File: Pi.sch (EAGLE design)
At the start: 9 parts, among them X1 RASPI_GPIO_B+#_BOX, X2 HDD, 5V 700mA

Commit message: Pi und Stromversorgung Rev. 2019
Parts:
- removed SV1: PLATINENVERBINDER-31SMD, homepi:PLATINENVERBINDER-31SMD
- added JP2: (no value), pinhead:PINHD-1X1
- added X3: MAC64L, con-vg:MAC64L
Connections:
- new net +24V: X3.A32, X3.C32
- new net +5V_EXT: X3.A31, X3.C31
- new net GND_EXT: X3.A30, X3.C30
- new net PI_RESET: JP2.1, X3.C7
- new net RXD: X1.RXD, X3.C27
- new net TXD: X1.TXD, X3.C26
- net +3,3V: now also X3.A2, X3.C2; no longer SV1.2
- net +5V_INT: now also X3.A1, X3.C1; no longer SV1.1
- net +5V_INT2: now also X3.A28, X3.C28; no longer SV1.28
- net 1WIRE: now also X3.A7; no longer SV1.7
- net GND_INT: now also X3.A29, X3.A3, X3.A6, X3.A8, X3.C29, X3.C3, X3.C6, X3.C8; no longer SV1.29, SV1.3, SV1.6, SV1.8
- net GPIO.05: now also X3.A14; no longer SV1.14
- net GPIO.06: now also X3.A15; no longer SV1.15
- net GPIO.12: now also X3.A16; no longer SV1.16
- net GPIO.13: now also X3.A17; no longer SV1.17
- net GPIO.16: now also X3.A18; no longer SV1.18
- net GPIO.17: now also X3.A19; no longer SV1.19
- net GPIO.18: now also X3.A20; no longer SV1.20
- net GPIO.19: now also X3.A21; no longer SV1.21
- net GPIO.20: now also X3.A22; no longer SV1.22
- net GPIO.21: now also X3.A23; no longer SV1.23
- net GPIO.22: now also X3.A24; no longer SV1.24
- net GPIO.23: now also X3.A25; no longer SV1.25
- net GPIO.24: now also X3.A26; no longer SV1.26
- net GPIO.25: now also X3.A27; no longer SV1.27
- net I2C_SCL: now also X3.A5; no longer SV1.5
- net I2C_SDA: now also X3.A4; no longer SV1.4
- net SPI_CE0: now also X3.A12; no longer SV1.12
- net SPI_CE1: now also X3.A13; no longer SV1.13
- net SPI_MISO: now also X3.A10; no longer SV1.10
- net SPI_MOSI: now also X3.A9; no longer SV1.9
- net SPI_SCLK: now also X3.A11; no longer SV1.11
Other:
- note added: "Einschubplatine für den Raspberry Pi Rev. 2019/03"
- moved on the sheet: JP1, LED1, LED2, R1, R2, RPI1, X2-1, X2-2

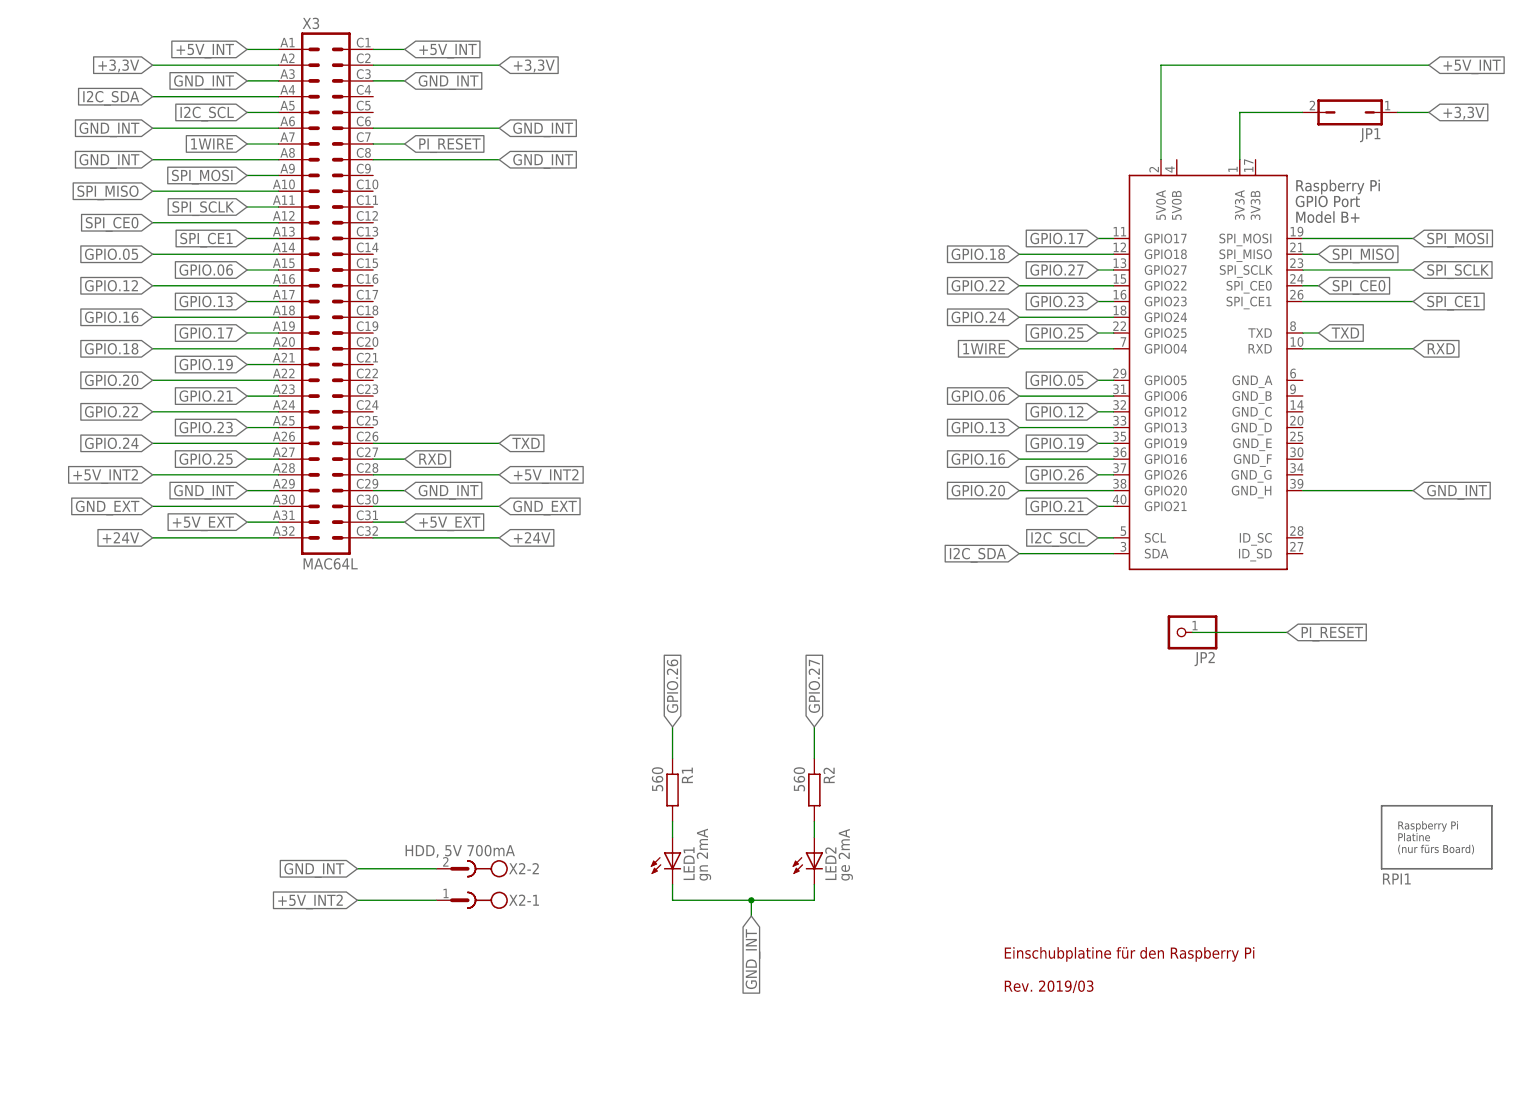
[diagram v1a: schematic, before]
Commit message: Anpassungen an Rev. 2019, erste Can-Bus Elemente
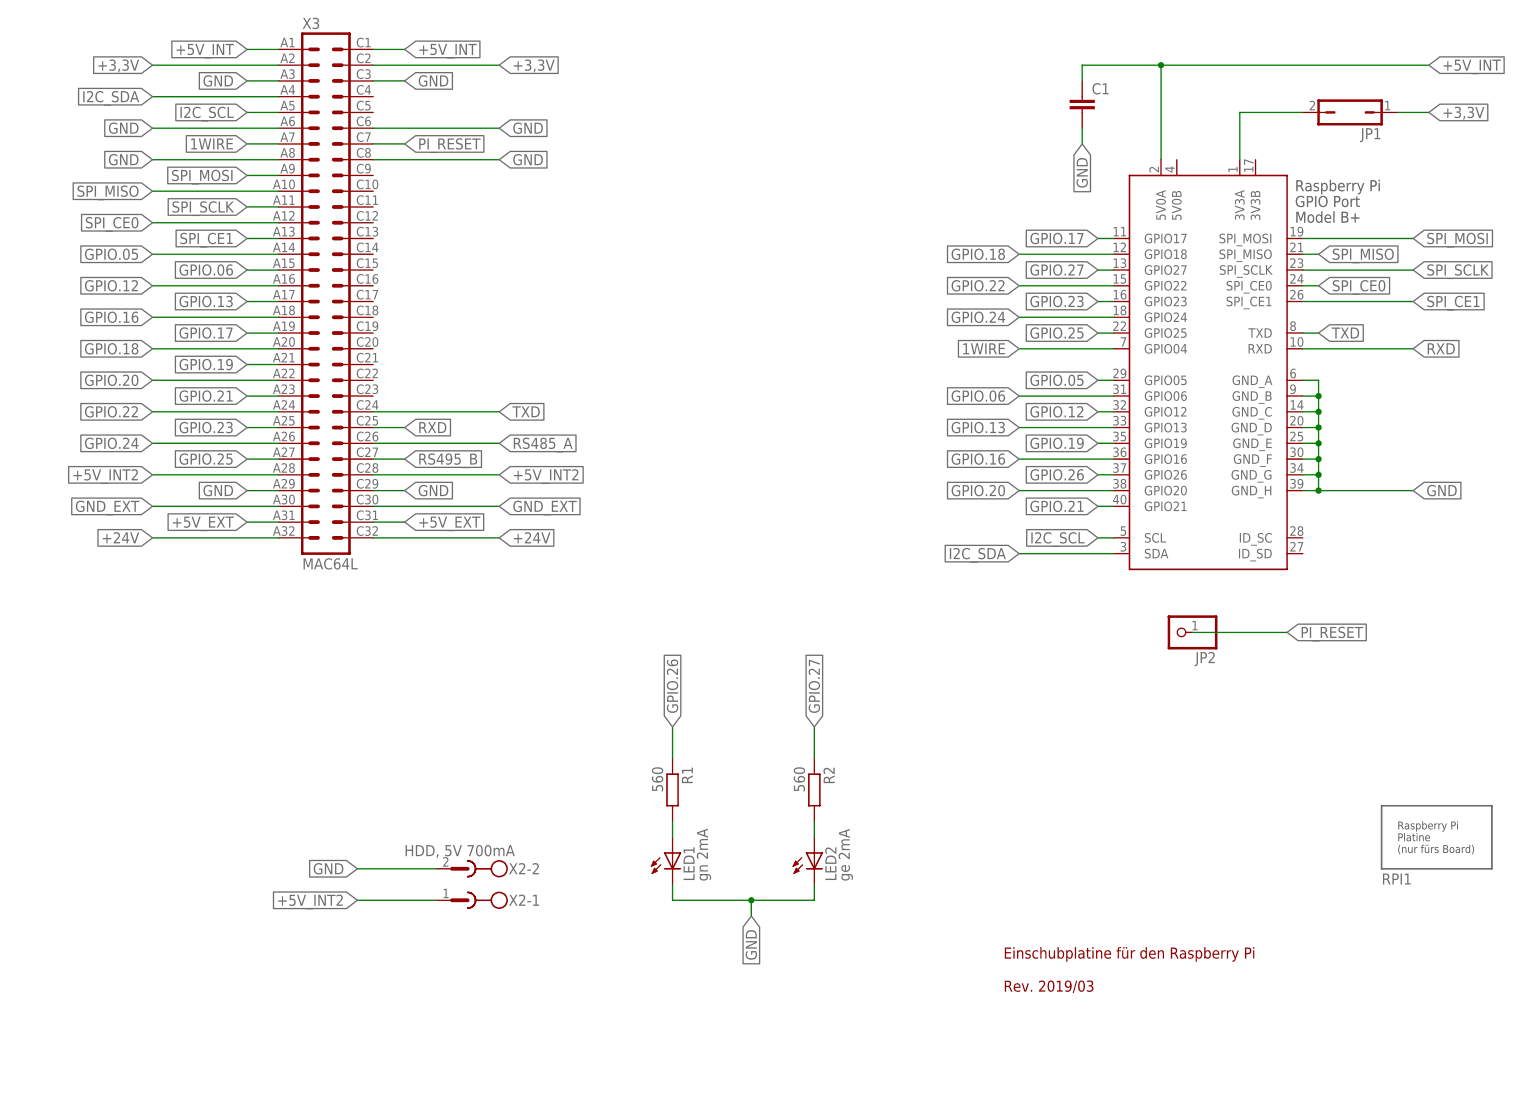
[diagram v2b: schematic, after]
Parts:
- added C1: (no value), rcl:C-EU050-024X044
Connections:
- removed net GND_INT: LED1.C, LED2.C, X1.GND_H, X2-2.1, X3.A29, X3.A3, X3.A6, X3.A8, X3.C29, X3.C3, X3.C6, X3.C8
- new net GND: C1.2, LED1.C, LED2.C, X1.GND_A, X1.GND_B, X1.GND_C, X1.GND_D, X1.GND_E, X1.GND_F, X1.GND_G, X1.GND_H, X2-2.1, X3.A29, X3.A3, X3.A6, X3.A8, X3.C29, X3.C3, X3.C6, X3.C8
- new net RS485_A: X3.C26
- new net RS495_B: X3.C27
- net +5V_INT: now also C1.1
- net RXD: now also X3.C25; no longer X3.C27
- net TXD: now also X3.C24; no longer X3.C26

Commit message: Can-Bus, Reset für den RasPi, Kleinere Optimierungen
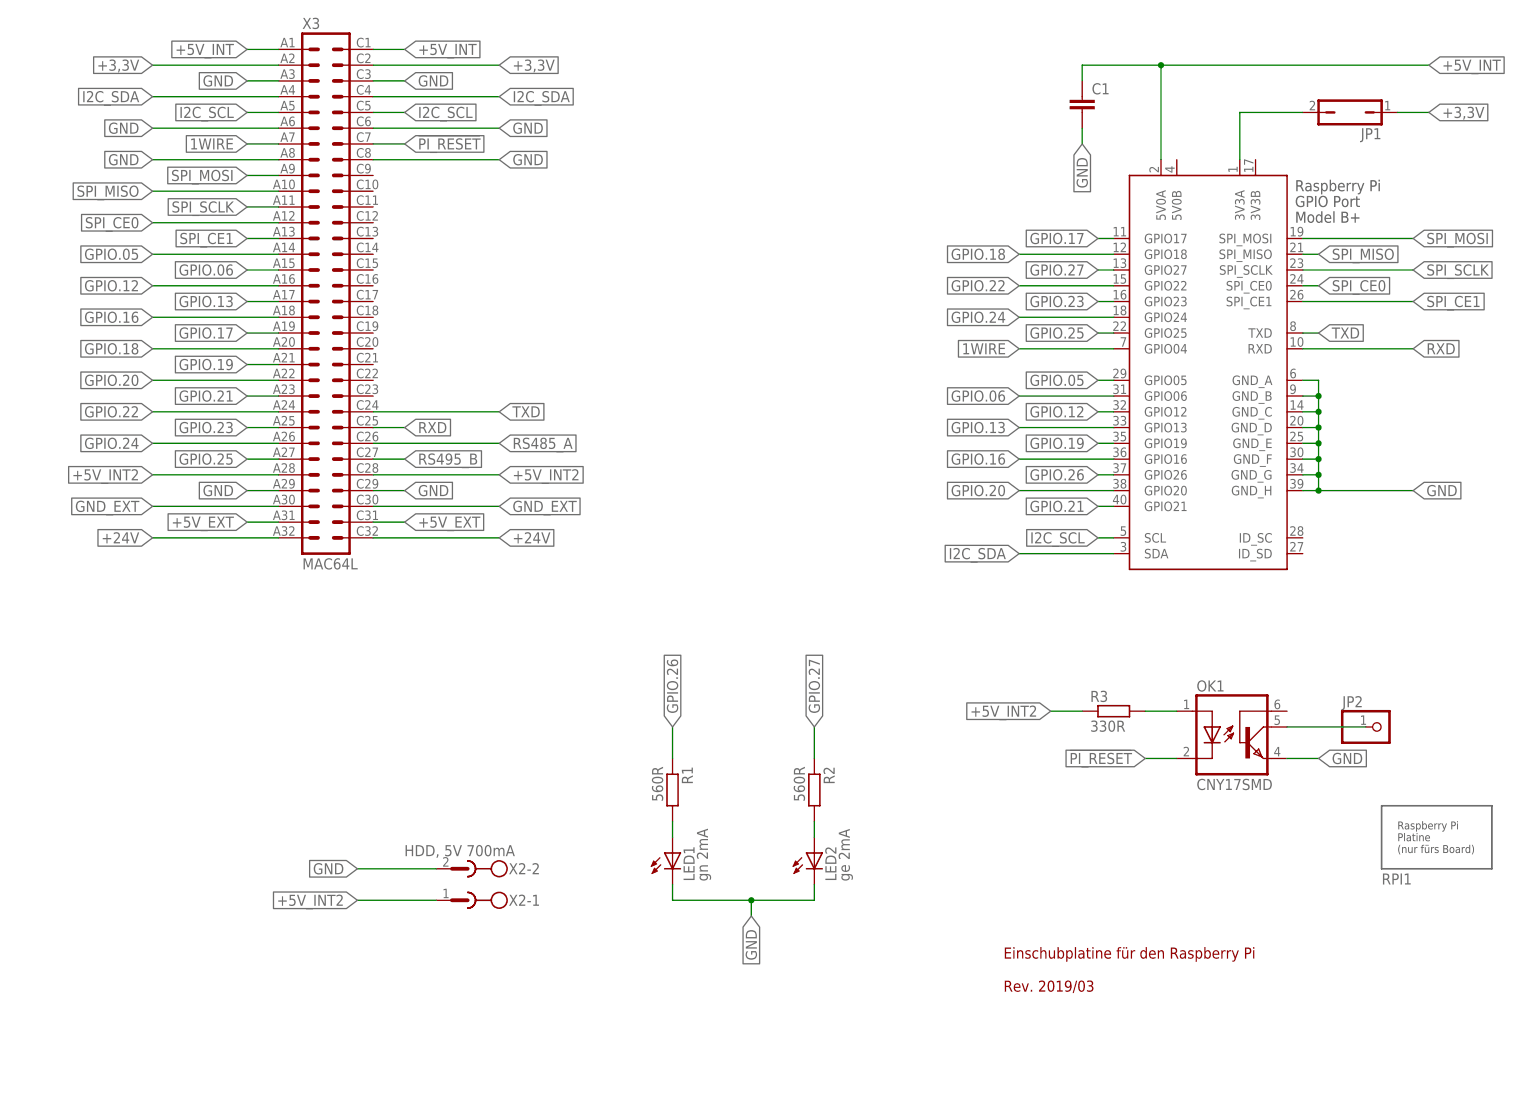
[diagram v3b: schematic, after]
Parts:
- added OK1: CNY17SMD, homepi:CNY17SMD
- added R3: 330R, rcl:R-EU_0204/5
- R1, R2: value 560 -> 560R
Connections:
- removed net PI_RESET: JP2.1, X3.C7
- new net !PI_RESET: OK1.C, X3.C7
- new net N$2: OK1.A, R3.2
- new net N$3: JP2.1, OK1.COL
- net +5V_INT2: now also R3.1
- net GND: now also OK1.EMI
- net I2C_SCL: now also X3.C5
- net I2C_SDA: now also X3.C4
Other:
- moved on the sheet: JP2
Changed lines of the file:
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@@
 <part name="RPI1" library="homepi" deviceset="RASPBERRYPI-PLATINE" device=""/>
 <part name="JP1" library="jumper" deviceset="JP1Q" device=""/>
-<part name="R1" library="rcl" deviceset="R-EU_" device="0204/7" value="560"/>
+<part name="R1" library="rcl" deviceset="R-EU_" device="0204/7" value="560R"/>
 <part name="LED1" library="led" deviceset="LED" device="3MM" value="gn 2mA"/>
-<part name="R2" library="rcl" deviceset="R-EU_" device="0204/7" value="560"/>
+<part name="R2" library="rcl" deviceset="R-EU_" device="0204/7" value="560R"/>
 <part name="LED2" library="led" deviceset="LED" device="3MM" value="ge 2mA"/>
 <part name="X2" library="con-phoenix-508" deviceset="MSTBV2" device="" value="HDD, 5V 700mA"/>
@@
 <part name="FRAME1" library="frames" deviceset="A4L-LOC" device=""/>
 <part name="C1" library="rcl" deviceset="C-EU" device="050-024X044"/>
+<part name="OK1" library="homepi" deviceset="CNY17" device="SMD"/>
+<part name="R3" library="rcl" deviceset="R-EU_" device="0204/5" value="330R"/>
 </parts>
 <sheets>
@@
 <instance part="X2" gate="-2" x="76.2" y="33.02" rot="R180"/>
 <instance part="X3" gate="G$1" x="53.34" y="127"/>
-<instance part="JP2" gate="G$1" x="190.5" y="71.12" rot="R180"/>
+<instance part="JP2" gate="G$1" x="223.52" y="55.88"/>
 <instance part="FRAME1" gate="G$1" x="0" y="0"/>
 <instance part="C1" gate="G$1" x="175.26" y="157.48"/>
+<instance part="OK1" gate="G$1" x="200.66" y="55.88"/>
+<instance part="R3" gate="G$1" x="180.34" y="58.42"/>
 </instances>
 <busses>
@@
 <label x="25.4" y="157.48" size="1.778" layer="95" rot="R180" xref="yes"/>
 </segment>
+<segment>
+<pinref part="X3" gate="G$1" pin="C4"/>
+<wire x1="60.96" y1="157.48" x2="81.28" y2="157.48" width="0.1524" layer="91"/>
+<label x="81.28" y="157.48" size="1.778" layer="95" xref="yes"/>
+</segment>
 </net>
 <net name="I2C_SCL" class="0">
@@
 <wire x1="45.72" y1="154.94" x2="40.64" y2="154.94" width="0.1524" layer="91"/>
 <label x="40.64" y="154.94" size="1.778" layer="95" rot="R180" xref="yes"/>
+</segment>
+<segment>
+<pinref part="X3" gate="G$1" pin="C5"/>
+<wire x1="60.96" y1="154.94" x2="66.04" y2="154.94" width="0.1524" layer="91"/>
+<label x="66.04" y="154.94" size="1.778" layer="95" xref="yes"/>
 </segment>
 </net>
@@
 <wire x1="60.96" y1="96.52" x2="81.28" y2="96.52" width="0.1524" layer="91"/>
 <label x="81.28" y="96.52" size="1.778" layer="95" xref="yes"/>
+</segment>
+<segment>
+<pinref part="R3" gate="G$1" pin="1"/>
+<wire x1="175.26" y1="58.42" x2="170.18" y2="58.42" width="0.1524" layer="91"/>
+<label x="170.18" y="58.42" size="1.778" layer="95" rot="R180" xref="yes"/>
 </segment>
 </net>
@@
 <wire x1="60.96" y1="106.68" x2="81.28" y2="106.68" width="0.1524" layer="91"/>
 <label x="81.28" y="106.68" size="1.778" layer="95" xref="yes"/>
-</segment>
-</net>
-<net name="PI_RESET" class="0">
-<segment>
-<pinref part="X3" gate="G$1" pin="C7"/>
-<wire x1="60.96" y1="149.86" x2="66.04" y2="149.86" width="0.1524" layer="91"/>
-<label x="66.04" y="149.86" size="1.778" layer="95" xref="yes"/>
-</segment>
-<segment>
-<pinref part="JP2" gate="G$1" pin="1"/>
-<wire x1="193.04" y1="71.12" x2="208.28" y2="71.12" width="0.1524" layer="91"/>
-<label x="208.28" y="71.12" size="1.778" layer="95" xref="yes"/>
 </segment>
 </net>
@@
 <label x="66.04" y="93.98" size="1.778" layer="95" xref="yes"/>
 </segment>
-</net>
+<segment>
+<pinref part="OK1" gate="G$1" pin="EMI"/>
+<wire x1="208.28" y1="50.8" x2="213.36" y2="50.8" width="0.1524" layer="91"/>
+<label x="213.36" y="50.8" size="1.778" layer="95" xref="yes"/>
+</segment>
+</net>
+<net name="N$2" class="0">
+<segment>
+<pinref part="R3" gate="G$1" pin="2"/>
+<pinref part="OK1" gate="G$1" pin="A"/>
+<wire x1="185.42" y1="58.42" x2="190.5" y2="58.42" width="0.1524" layer="91"/>
+</segment>
+</net>
+<net name="N$3" class="0">
+<segment>
+<pinref part="JP2" gate="G$1" pin="1"/>
+<pinref part="OK1" gate="G$1" pin="COL"/>
+<wire x1="220.98" y1="55.88" x2="208.28" y2="55.88" width="0.1524" layer="91"/>
+</segment>
+</net>
+<net name="!PI_RESET" class="0">
+<segment>
+<pinref part="OK1" gate="G$1" pin="C"/>
+<wire x1="190.5" y1="50.8" x2="185.42" y2="50.8" width="0.1524" layer="91"/>
+<label x="185.42" y="50.8" size="1.778" layer="95" rot="R180" xref="yes"/>
+</segment>
+<segment>
+<pinref part="X3" gate="G$1" pin="C7"/>
+<wire x1="60.96" y1="149.86" x2="66.04" y2="149.86" width="0.1524" layer="91"/>
+<label x="66.04" y="149.86" size="1.778" layer="95" xref="yes"/>
+</segment>
+</net>

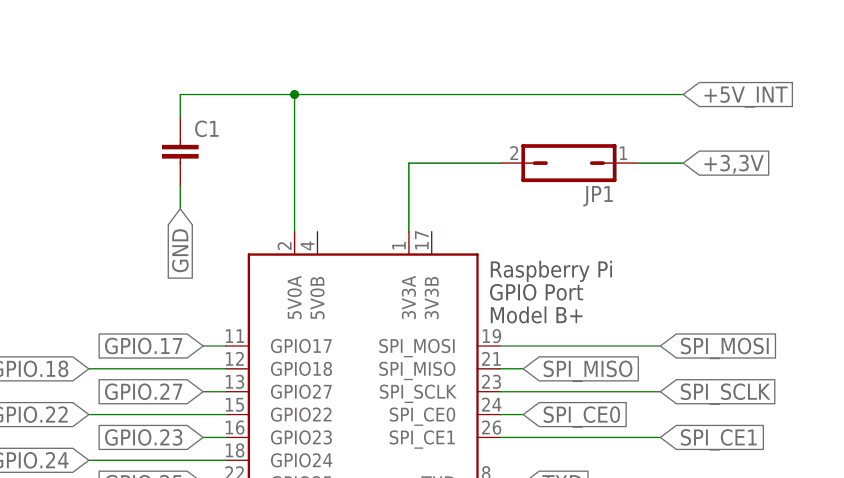
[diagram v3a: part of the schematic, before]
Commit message: 3,3V-Versorgung nur noch über TSR-Spannungsregler
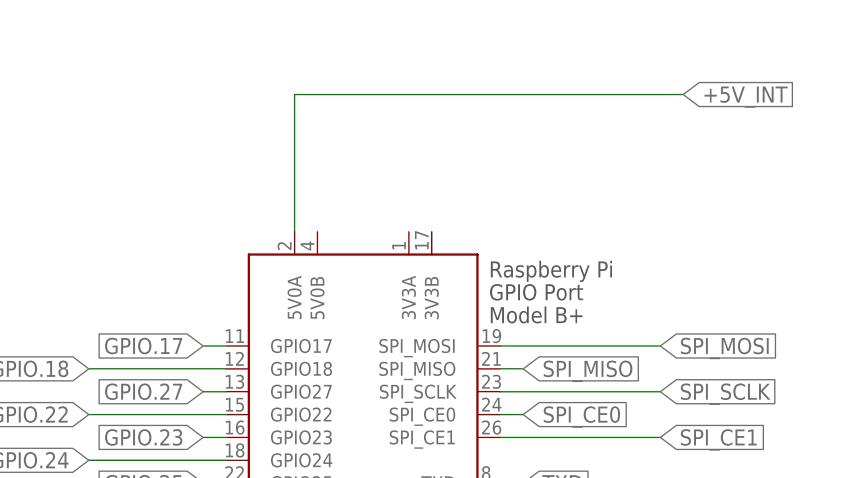
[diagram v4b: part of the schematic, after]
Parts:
- removed C1: (no value), rcl:C-EU050-024X044
- removed JP1: (no value), jumper:JP1Q
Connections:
- removed net N$9: JP1.2, X1.3V3A
- net +3,3V: no longer JP1.1
- net +5V_INT: no longer C1.1
- net GND: no longer C1.2
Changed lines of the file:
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@@
 <part name="X1" library="raspberrypi_bastelstube_v13" deviceset="RASPI_GPIO_B+#" device="_BOX"/>
 <part name="RPI1" library="homepi" deviceset="RASPBERRYPI-PLATINE" device=""/>
-<part name="JP1" library="jumper" deviceset="JP1Q" device=""/>
 <part name="R1" library="rcl" deviceset="R-EU_" device="0204/7" value="560R"/>
 <part name="LED1" library="led" deviceset="LED" device="3MM" value="gn 2mA"/>
@@
 <part name="JP2" library="pinhead" deviceset="PINHD-1X1" device=""/>
 <part name="FRAME1" library="frames" deviceset="A4L-LOC" device=""/>
-<part name="C1" library="rcl" deviceset="C-EU" device="050-024X044"/>
 <part name="OK1" library="homepi" deviceset="CNY17" device="SMD"/>
 <part name="R3" library="rcl" deviceset="R-EU_" device="0204/5" value="330R"/>
@@
 <instance part="X1" gate="G$1" x="195.58" y="119.38"/>
 <instance part="RPI1" gate="G$1" x="223.52" y="33.02"/>
-<instance part="JP1" gate="A" x="218.44" y="154.94" rot="R90"/>
 <instance part="R1" gate="G$1" x="109.22" y="45.72" rot="R270"/>
 <instance part="LED1" gate="G$1" x="109.22" y="35.56"/>
@@
 <instance part="JP2" gate="G$1" x="223.52" y="55.88"/>
 <instance part="FRAME1" gate="G$1" x="0" y="0"/>
-<instance part="C1" gate="G$1" x="175.26" y="157.48"/>
 <instance part="OK1" gate="G$1" x="200.66" y="55.88"/>
 <instance part="R3" gate="G$1" x="180.34" y="58.42"/>
@@
 </segment>
 </net>
-<net name="N$9" class="0">
-<segment>
-<pinref part="X1" gate="G$1" pin="3V3A"/>
-<pinref part="JP1" gate="A" pin="2"/>
-<wire x1="200.66" y1="147.32" x2="200.66" y2="154.94" width="0.1524" layer="91"/>
-<wire x1="200.66" y1="154.94" x2="210.82" y2="154.94" width="0.1524" layer="91"/>
-</segment>
-</net>
 <net name="+3,3V" class="0">
-<segment>
-<pinref part="JP1" gate="A" pin="1"/>
-<wire x1="226.06" y1="154.94" x2="231.14" y2="154.94" width="0.1524" layer="91"/>
-<label x="231.14" y="154.94" size="1.778" layer="95" xref="yes"/>
-</segment>
 <segment>
 <pinref part="X3" gate="G$1" pin="A2"/>
@@
 <wire x1="187.96" y1="162.56" x2="231.14" y2="162.56" width="0.1524" layer="91"/>
 <label x="231.14" y="162.56" size="1.778" layer="95" xref="yes"/>
-<pinref part="C1" gate="G$1" pin="1"/>
-<wire x1="187.96" y1="162.56" x2="175.26" y2="162.56" width="0.1524" layer="91"/>
-<wire x1="175.26" y1="162.56" x2="175.26" y2="160.02" width="0.1524" layer="91"/>
-<junction x="187.96" y="162.56"/>
 </segment>
 <segment>
@@
 <net name="GND" class="0">
 <segment>
-<pinref part="C1" gate="G$1" pin="2"/>
-<wire x1="175.26" y1="152.4" x2="175.26" y2="149.86" width="0.1524" layer="91"/>
-<label x="175.26" y="149.86" size="1.778" layer="95" rot="R270" xref="yes"/>
-</segment>
-<segment>
 <pinref part="X2" gate="-2" pin="1"/>
